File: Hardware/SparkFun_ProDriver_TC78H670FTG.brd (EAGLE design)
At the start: 50.8 x 57.1 mm, 137 parts, among them J2 LATCH, J3 PTH, J4 LATCH, J5 LATCH, J6 PTH, J7 LATCH, J8 PTH, U1 TC78H670FTG, U2 LM1117

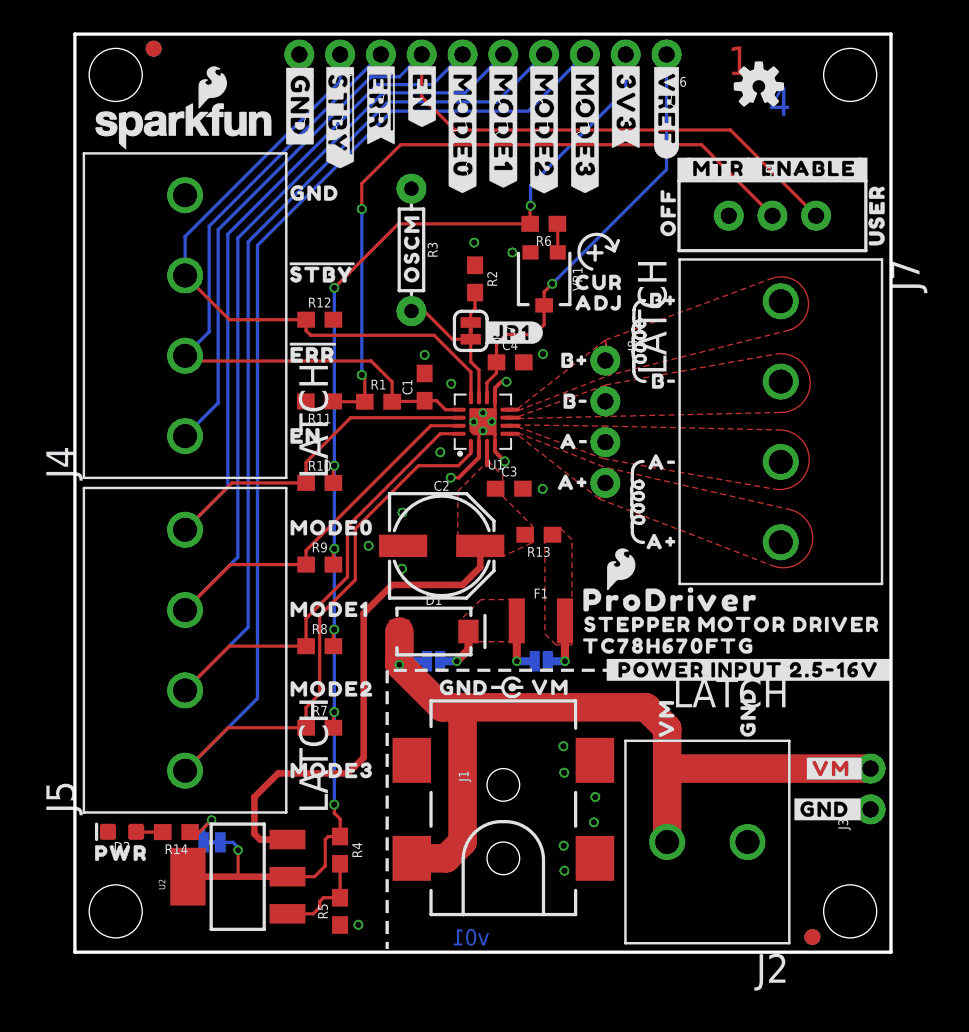
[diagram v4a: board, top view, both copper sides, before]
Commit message: Suggestions from design review
-Jumper names same in sch and brd labels
-JP1 to OSCM
-ERR net position aligned with others
-changed power input silk to 3.3V-16V, also updated sch
-added more vias near IC, head sink exposed copper, and VM input traces to help heat transfer to inner layers.
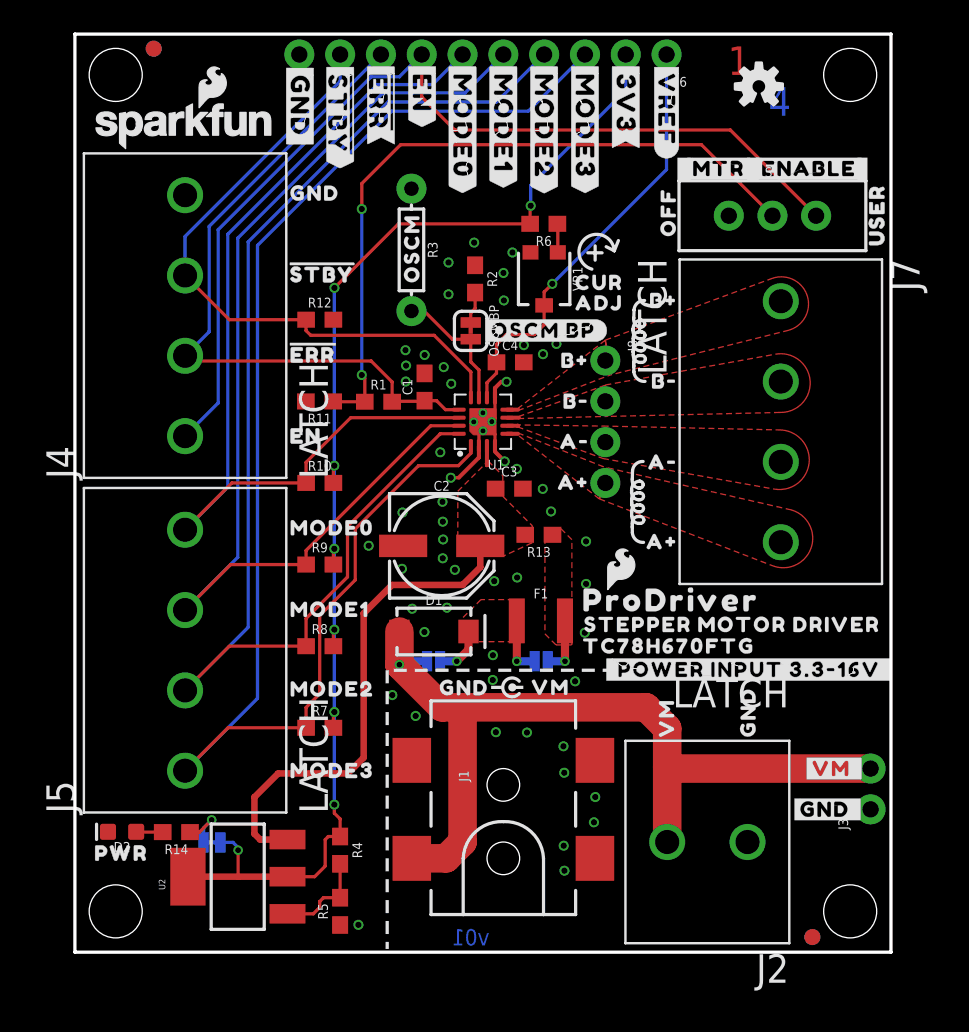
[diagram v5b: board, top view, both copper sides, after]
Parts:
- removed U$41: (no value), output:#_POWER_INPUT_2#5#16V_#0
- added U$16: (no value), output:#OSCM_BP#0
- U$45: device output:#JP1#0 -> output:#_POWER_INPUT_3#3#16V_#0
- moved U$45 22.3 mm to (32.8, 17.6)
- renumbered JP1 to OSCMBP, JP2 to PTCBP, JP3 to D1BP
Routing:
- net GND: vias 24 -> 56
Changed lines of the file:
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@@
 <layer number="28" name="bValues" color="7" fill="1" visible="no" active="yes"/>
 <layer number="29" name="tStop" color="30" fill="5" visible="no" active="yes"/>
-<layer number="30" name="bStop" color="7" fill="6" visible="no" active="yes"/>
+<layer number="30" name="bStop" color="7" fill="6" visible="yes" active="yes"/>
 <layer number="31" name="tCream" color="7" fill="4" visible="no" active="yes"/>
 <layer number="32" name="bCream" color="7" fill="5" visible="no" active="yes"/>
@@
 <attribute name="VALUE" x="19.93391875" y="43.71848125" size="0.6096" layer="27" font="vector" ratio="20" rot="R270" align="top-center"/>
 </element>
-<element name="JP1" library="SparkFun-Jumpers" package="SMT-JUMPER_2_NC_TRACE_SILK" package3d_urn="urn:adsk.eagle:package:39281/1" value="" x="24.6405375" y="38.676578125" smashed="yes" rot="R270">
+<element name="OSCMBP" library="SparkFun-Jumpers" package="SMT-JUMPER_2_NC_TRACE_SILK" package3d_urn="urn:adsk.eagle:package:39281/1" value="" x="24.6405375" y="38.676578125" smashed="yes" rot="R270">
 <attribute name="NAME" x="25.7835375" y="38.676578125" size="0.6096" layer="25" font="vector" ratio="20" rot="R270" align="bottom-center"/>
 <attribute name="VALUE" x="23.4975375" y="38.676578125" size="0.6096" layer="27" font="vector" ratio="20" rot="R270" align="top-center"/>
@@
 <element name="U$31" library="output" package="#GND#0" value="" x="14.0081" y="52.6694375" smashed="yes" rot="R270"/>
 <element name="U$40" library="output" package="PRODRIVER0" value="" x="30.55619375" y="21.91765625" smashed="yes"/>
-<element name="U$41" library="output" package="#_POWER_INPUT_2#5#16V_#0" value="" x="32.766" y="17.571721875" smashed="yes"/>
 <element name="U$14" library="output" package="#MTR#0" value="" x="37.7571" y="48.77815625" smashed="yes"/>
 <element name="U$21" library="output" package="#ENABLE#0" value="" x="42.0497" y="48.77815625" smashed="yes"/>
@@
 <element name="U$43" library="output" package="A#3" value="" x="32.717740625" y="31.783021875" smashed="yes"/>
 <element name="U$44" library="output" package="A#2" value="" x="32.6923375" y="29.24048125" smashed="yes"/>
-<element name="U$45" library="output" package="#JP1#0" value="" x="25.313640625" y="38.56481875" smashed="yes"/>
 <element name="U$19" library="output" package="EN0" value="" x="12.7" y="32.131" smashed="yes"/>
 <element name="U$13" library="output" package="#EN#2" value="" x="21.6154" y="55.5498" smashed="yes" rot="R270"/>
@@
 <attribute name="VALUE" x="28.8798" y="26.7462" size="0.6096" layer="27" font="vector" ratio="20" rot="R180" align="top-center"/>
 </element>
-<element name="JP2" library="SparkFun-Jumpers" library_urn="urn:adsk.eagle:library:528" package="SMT-JUMPER_2_NO_SILK" package3d_urn="urn:adsk.eagle:package:39279/1" value="" x="29.0322" y="18.1102" smashed="yes" rot="MR180">
+<element name="PTCBP" library="SparkFun-Jumpers" library_urn="urn:adsk.eagle:library:528" package="SMT-JUMPER_2_NO_SILK" package3d_urn="urn:adsk.eagle:package:39279/1" value="" x="29.0322" y="18.1102" smashed="yes" rot="MR180">
 <attribute name="NAME" x="29.0322" y="16.9672" size="0.6096" layer="26" font="vector" ratio="20" rot="MR180" align="bottom-center"/>
 <attribute name="VALUE" x="29.0322" y="19.2532" size="0.6096" layer="28" font="vector" ratio="20" rot="MR180" align="top-center"/>
 </element>
-<element name="JP3" library="SparkFun-Jumpers" library_urn="urn:adsk.eagle:library:528" package="SMT-JUMPER_2_NO_SILK" package3d_urn="urn:adsk.eagle:package:39279/1" value="" x="22.3266" y="18.1102" smashed="yes" rot="MR180">
+<element name="D1BP" library="SparkFun-Jumpers" library_urn="urn:adsk.eagle:library:528" package="SMT-JUMPER_2_NO_SILK" package3d_urn="urn:adsk.eagle:package:39279/1" value="" x="22.3266" y="18.1102" smashed="yes" rot="MR180">
 <attribute name="NAME" x="22.3266" y="16.9672" size="0.6096" layer="26" font="vector" ratio="20" rot="MR180" align="bottom-center"/>
 <attribute name="VALUE" x="22.3266" y="19.2532" size="0.6096" layer="28" font="vector" ratio="20" rot="MR180" align="top-center"/>
@@
 <element name="U$54" library="output" package="##ERR##6" value="" x="19.05" y="55.547259375" smashed="yes" rot="MR270"/>
 <element name="U$7" library="output" package="USER0" value="" x="49.9237" y="43.2816" smashed="yes" rot="R90"/>
+<element name="U$16" library="output" package="#OSCM_BP#0" value="" x="25.229821875" y="38.6994375" smashed="yes"/>
+<element name="U$45" library="output" package="#_POWER_INPUT_3#3#16V_#0" value="" x="32.7533" y="17.592040625" smashed="yes"/>
 </elements>
 <signals>
@@
 <contactref element="R12" pad="2"/>
 <contactref element="R11" pad="2"/>
+<via x="22.882859375" y="28.036521875" extent="1-16" drill="0.381"/>
+<via x="22.903178125" y="26.799540625" extent="1-16" drill="0.381"/>
+<via x="22.920959375" y="25.6921" extent="1-16" drill="0.381"/>
+<via x="22.8981" y="24.518621875" extent="1-16" drill="0.381"/>
+<via x="23.652478125" y="23.802340625" extent="1-16" drill="0.381"/>
+<via x="27.513278125" y="30.083759375" extent="1-16" drill="0.381"/>
+<via x="20.59431875" y="35.5219" extent="1-16" drill="0.381"/>
+<via x="20.614640625" y="36.515040625" extent="1-16" drill="0.381"/>
+<via x="20.576540625" y="37.472621875" extent="1-16" drill="0.381"/>
+<via x="22.959059375" y="36.421059375" extent="1-16" drill="0.381"/>
+<via x="27.94761875" y="37.790121875" extent="1-16" drill="0.381"/>
+<via x="29.974540625" y="37.866321875" extent="1-16" drill="0.381"/>
+<via x="26.0096" y="16.94688125" extent="1-16" drill="0.381"/>
+<via x="31.137859375" y="16.860521875" extent="1-16" drill="0.381"/>
+<via x="28.140659375" y="13.672821875" extent="1-16" drill="0.381"/>
+<via x="26.20518125" y="13.69568125" extent="1-16" drill="0.381"/>
+<via x="19.758659375" y="16.004540625" extent="1-16" drill="0.381"/>
+<via x="21.211540625" y="14.7066" extent="1-16" drill="0.381"/>
+<via x="26.67761875" y="42.280840625" extent="1-16" drill="0.381"/>
+<via x="26.70048125" y="40.571421875" extent="1-16" drill="0.381"/>
+<via x="23.256240625" y="40.952421875" extent="1-16" drill="0.381"/>
+<via x="23.256240625" y="42.933621875" extent="1-16" drill="0.381"/>
+<via x="27.52851875" y="23.319740625" extent="1-16" drill="0.381"/>
+<via x="26.101040625" y="23.096221875" extent="1-16" drill="0.381"/>
+<via x="23.15718125" y="21.445221875" extent="1-16" drill="0.381"/>
+<via x="20.9931" y="21.381721875" extent="1-16" drill="0.381"/>
+<via x="21.757640625" y="19.928840625" extent="1-16" drill="0.381"/>
+<via x="26.019759375" y="18.4886625" extent="1-16" drill="0.381"/>
+<via x="31.739840625" y="19.8882" extent="1-16" drill="0.381"/>
+<via x="31.81858125" y="22.9235" extent="1-16" drill="0.381"/>
+<via x="31.81858125" y="25.57018125" extent="1-16" drill="0.381"/>
+<via x="29.639259375" y="27.43708125" extent="1-16" drill="0.381"/>
 </signal>
 <signal name="N$30">
@@
 <signal name="OSCM">
 <contactref element="U1" pad="11"/>
-<contactref element="JP1" pad="2"/>
+<contactref element="OSCMBP" pad="2"/>
 <contactref element="R3" pad="P$2"/>
 <wire x1="25.15" y1="34.526" x2="25.15" y2="36.2418" width="0.2032" layer="1"/>
@@
 <signal name="N$2">
 <contactref element="R2" pad="2"/>
-<contactref element="JP1" pad="1"/>
+<contactref element="OSCMBP" pad="1"/>
 <wire x1="24.6405375" y1="39.197278125" x2="24.6405375" y2="39.794178125" width="0.2032" layer="1"/>
 <wire x1="24.912321875" y1="40.0659625" x2="24.912321875" y2="41.06" width="0.2032" layer="1"/>
@@
 <wire x1="24.13" y1="15.24" x2="24.13" y2="6.858" width="1.778" layer="1"/>
 <wire x1="24.13" y1="6.858" x2="23.114" y2="5.842" width="1.778" layer="1"/>
-<contactref element="JP3" pad="1"/>
+<contactref element="D1BP" pad="1"/>
 <wire x1="21.9202" y1="18.1102" x2="20.40911875" y2="18.1102" width="0.508" layer="16"/>
 <wire x1="20.40911875" y1="18.1102" x2="20.199459375" y2="17.900540625" width="0.508" layer="16"/>
@@
 <contactref element="D1" pad="C"/>
 <contactref element="F1" pad="1"/>
-<contactref element="JP3" pad="2"/>
-<contactref element="JP2" pad="1"/>
+<contactref element="D1BP" pad="2"/>
+<contactref element="PTCBP" pad="1"/>
 <wire x1="27.5068" y1="20.6248" x2="27.5068" y2="18.1116" width="0.508" layer="1"/>
 <wire x1="27.5068" y1="18.1116" x2="27.5082" y2="18.1102" width="0.508" layer="1"/>
@@
 <signal name="N$3">
 <contactref element="F1" pad="2"/>
-<contactref element="JP2" pad="2"/>
+<contactref element="PTCBP" pad="2"/>
 <contactref element="R13" pad="1"/>
 <polygon width="0.2032" layer="1" thermals="no">

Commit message: Double-check fixes
-Eagle Library had storefront SKUs for latch terminals. Corrected to prod IDs.
-removed unnecessary flame symbol in sch (lcopied a second footprint to keep in board).
-text font to vector on one sch paragraph
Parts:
- renumbered LOGO4 to LOGO6
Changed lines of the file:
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@@
 <attribute name="REV" value="" x="-2.54" y="-16.51" size="1.778" layer="27" display="off"/>
 </element>
-<element name="LOGO4" library="SparkFun-Aesthetics" package="SFE_LOGO_FLAME_.1" value="SFE_LOGO_FLAME.1_INCH" x="33.99028125" y="23.860753125" smashed="yes"/>
 <element name="FID3" library="SparkFun-Aesthetics" package="FIDUCIAL-1X2" value="FIDUCIAL1X2" x="4.904740625" y="56.243221875" smashed="yes" rot="MR0"/>
 <element name="FID4" library="SparkFun-Aesthetics" package="FIDUCIAL-1X2" value="FIDUCIAL1X2" x="45.907959375" y="0.942340625" smashed="yes" rot="MR0"/>
 <element name="J5" library="SparkFun-Connectors" package="LATCHTERMINAL-5MM-4" value="LATCH" x="6.858" y="18.796" smashed="yes" rot="R90">
 <attribute name="NAME" x="0" y="8.636" size="1.778" layer="25" rot="R90"/>
-<attribute name="PROD_ID" value="PRT-15900" x="6.858" y="18.796" size="1.778" layer="27" font="vector" ratio="15" rot="R90" display="off"/>
+<attribute name="PROD_ID" value="CONN-14722" x="6.858" y="18.796" size="1.778" layer="27" font="vector" ratio="15" rot="R90" display="off"/>
+<attribute name="STOREFRONT_SKU" value="PRT-15900" x="6.858" y="18.796" size="1.778" layer="27" rot="R90" display="off"/>
 <attribute name="VALUE" x="15.748" y="8.636" size="1.778" layer="25" rot="R90"/>
 </element>
 <element name="J2" library="SparkFun-Connectors" package="LATCHTERMINAL-5MM-2" value="LATCH" x="39.37" y="6.858" smashed="yes" rot="R180">
 <attribute name="NAME" x="44.45" y="-0.127" size="1.778" layer="25" rot="R180"/>
-<attribute name="PROD_ID" value="PRT-15898" x="39.37" y="6.858" size="1.778" layer="27" font="vector" ratio="15" rot="R180" display="off"/>
+<attribute name="PROD_ID" value="CONN-14720" x="39.37" y="6.858" size="1.778" layer="27" font="vector" ratio="15" rot="R180" display="off"/>
+<attribute name="STOREFRONT_SKU" value="PRT-15898" x="39.37" y="6.858" size="1.778" layer="27" rot="R180" display="off"/>
 <attribute name="VALUE" x="44.45" y="17.018" size="1.778" layer="25" rot="R180"/>
 </element>
@@
 <element name="J7" library="SparkFun-Connectors" package="LATCHTERMINAL-5MM-4" value="LATCH" x="43.942" y="33.02" smashed="yes" rot="R270">
 <attribute name="NAME" x="50.8" y="43.18" size="1.778" layer="25" rot="R270"/>
-<attribute name="PROD_ID" value="PRT-15900" x="43.942" y="33.02" size="1.778" layer="27" font="vector" ratio="15" rot="R270" display="off"/>
+<attribute name="PROD_ID" value="CONN-14722" x="43.942" y="33.02" size="1.778" layer="27" font="vector" ratio="15" rot="R270" display="off"/>
+<attribute name="STOREFRONT_SKU" value="PRT-15900" x="43.942" y="33.02" size="1.778" layer="27" rot="R270" display="off"/>
 <attribute name="VALUE" x="35.052" y="43.18" size="1.778" layer="25" rot="R270"/>
 </element>
@@
 <element name="J4" library="SparkFun-Connectors" package="LATCHTERMINAL-5MM-4" value="LATCH" x="6.858" y="39.624" smashed="yes" rot="R90">
 <attribute name="NAME" x="0" y="29.464" size="1.778" layer="25" rot="R90"/>
-<attribute name="PROD_ID" value="PRT-15900" x="6.858" y="39.624" size="1.778" layer="27" font="vector" ratio="15" rot="R90" display="off"/>
+<attribute name="PROD_ID" value="CONN-14722" x="6.858" y="39.624" size="1.778" layer="27" font="vector" ratio="15" rot="R90" display="off"/>
+<attribute name="STOREFRONT_SKU" value="PRT-15900" x="6.858" y="39.624" size="1.778" layer="27" rot="R90" display="off"/>
 <attribute name="VALUE" x="15.748" y="29.464" size="1.778" layer="25" rot="R90"/>
 </element>
@@
 <element name="U$16" library="output" package="#OSCM_BP#0" value="" x="25.229821875" y="38.6994375" smashed="yes"/>
 <element name="U$45" library="output" package="#_POWER_INPUT_3#3#16V_#0" value="" x="32.7533" y="17.592040625" smashed="yes"/>
+<element name="LOGO6" library="SparkFun-Aesthetics" package="SFE_LOGO_FLAME_.1" value="SFE_LOGO_FLAME.1_INCH" x="33.99028125" y="23.860753125" smashed="yes"/>
 </elements>
 <signals>

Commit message: added dummy traces to 2/15, removed bottom paste on IC package
-Added some dummy traces to 2/15 inner layers so the CAMmer tool will pick up on them and create gerbers.
-There was some bottom paste on the IC footprint I never noticed till reviewing gerbers, I think this was left over from the QFN footprint I started from.
-Also updated preview jpgs to reflect most recent design.
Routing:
- net N$9: track 0.00 -> 1.50 mm
- net N$12: track 0.00 -> 1.25 mm
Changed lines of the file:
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@@
 <layer number="28" name="bValues" color="7" fill="1" visible="no" active="yes"/>
 <layer number="29" name="tStop" color="30" fill="5" visible="no" active="yes"/>
-<layer number="30" name="bStop" color="7" fill="6" visible="yes" active="yes"/>
+<layer number="30" name="bStop" color="7" fill="6" visible="no" active="yes"/>
 <layer number="31" name="tCream" color="7" fill="4" visible="no" active="yes"/>
 <layer number="32" name="bCream" color="7" fill="5" visible="no" active="yes"/>
@@
 <layer number="95" name="Names" color="7" fill="1" visible="no" active="no"/>
 <layer number="96" name="Values" color="7" fill="1" visible="no" active="no"/>
-<layer number="2" name="GND2" color="14" fill="1" visible="no" active="yes"/>
+<layer number="2" name="GND2" color="13" fill="6" visible="no" active="yes"/>
 <layer number="3" name="Route3" color="4" fill="3" visible="no" active="no"/>
 <layer number="4" name="Route4" color="1" fill="4" visible="no" active="no"/>
@@
 <layer number="13" name="Route13" color="4" fill="5" visible="no" active="no"/>
 <layer number="14" name="Route14" color="1" fill="6" visible="no" active="no"/>
-<layer number="15" name="GND15" color="13" fill="1" visible="no" active="yes"/>
+<layer number="15" name="GND15" color="14" fill="3" visible="no" active="yes"/>
 <layer number="53" name="tGND_GNDA" color="7" fill="9" visible="no" active="no"/>
 <layer number="54" name="bGND_GNDA" color="1" fill="9" visible="no" active="no"/>
@@
 <wire x1="39.0017" y1="50.264059375" x2="43.421303125" y2="45.84445625" width="0.2032" layer="1"/>
 </signal>
+<signal name="N$12">
+<wire x1="40.674290625" y1="51.76011875" x2="41.926509375" y2="51.76011875" width="0.254" layer="15"/>
+</signal>
+<signal name="N$9">
+<wire x1="43.119040625" y1="54.2544" x2="44.615103125" y2="54.2544" width="0.254" layer="2"/>
+</signal>
 </signals>
